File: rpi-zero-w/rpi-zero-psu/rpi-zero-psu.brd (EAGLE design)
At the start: 58 x 30 mm, 21 parts, among them J1 M20X2, J2 POWER_JACKPTH, Q1 DMG2305UX, Q2 DMG2302UK-7, U2 MP2307-MODULE, U4 DMMT5401

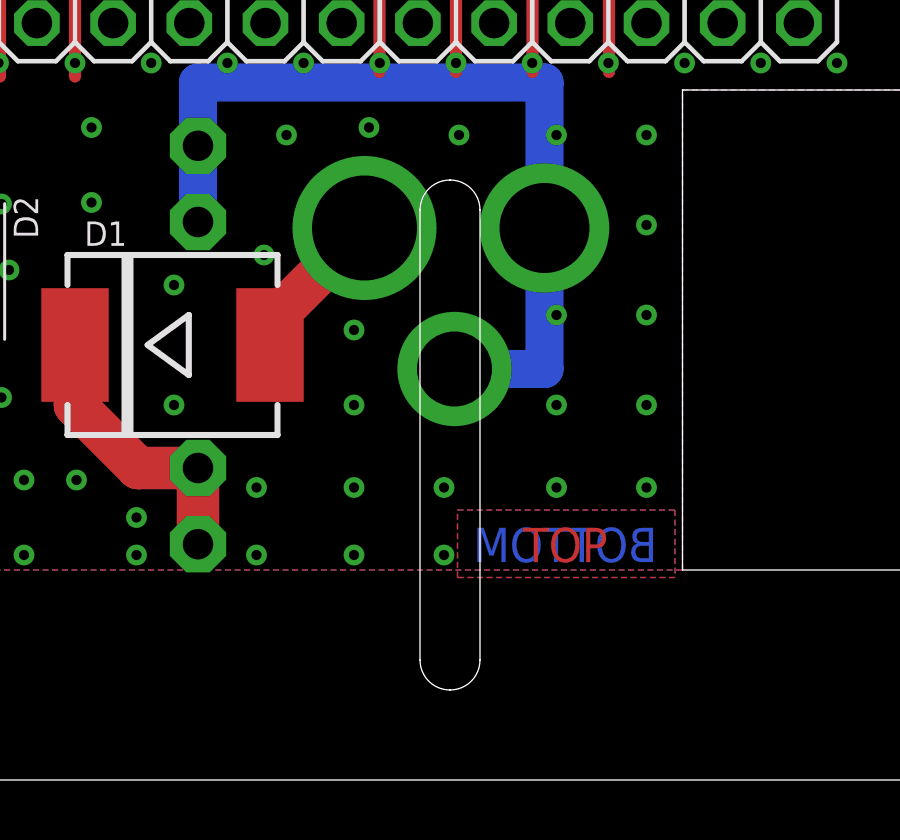
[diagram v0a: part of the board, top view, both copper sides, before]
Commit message: rpi-zero-psu: removed milling layer
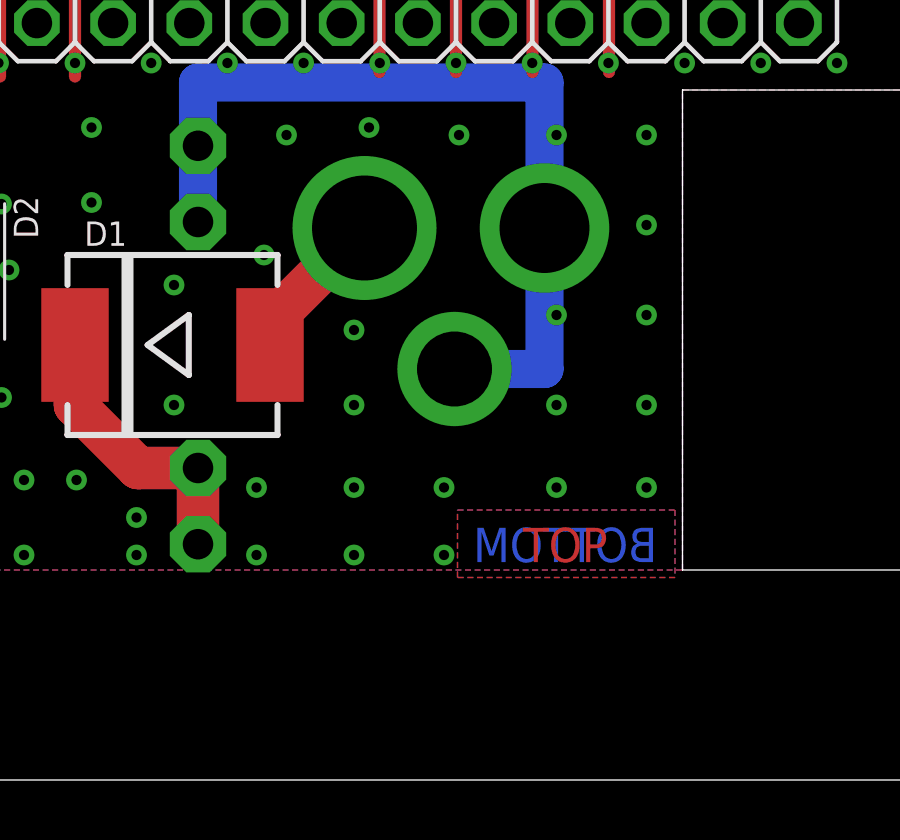
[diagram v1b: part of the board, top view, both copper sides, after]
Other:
- outline, holes or cut-outs redrawn
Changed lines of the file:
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@@
 <layer number="44" name="Drills" color="7" fill="1" visible="no" active="yes"/>
 <layer number="45" name="Holes" color="7" fill="1" visible="yes" active="yes"/>
-<layer number="46" name="Milling" color="3" fill="1" visible="no" active="yes"/>
+<layer number="46" name="Milling" color="3" fill="1" visible="yes" active="yes"/>
 <layer number="47" name="Measures" color="7" fill="1" visible="no" active="yes"/>
 <layer number="48" name="Document" color="7" fill="1" visible="no" active="yes"/>
@@
 <circle x="61.5" y="3.5" radius="1.55" width="3.1" layer="42"/>
 <circle x="61.5" y="26.5" radius="1.55" width="3.1" layer="42"/>
-<wire x1="44" y1="19" x2="44" y2="4" width="0" layer="46"/>
-<wire x1="46" y1="4" x2="45" y2="3" width="0" layer="46" curve="-90"/>
-<wire x1="44" y1="4" x2="45" y2="3" width="0" layer="46" curve="90"/>
-<wire x1="45" y1="20" x2="44" y2="19" width="0" layer="46" curve="90"/>
-<wire x1="45" y1="20" x2="46" y2="19" width="0" layer="46" curve="-90"/>
-<wire x1="46" y1="19" x2="46" y2="4" width="0" layer="46"/>
 <text x="57.25" y="0.75" size="1.016" layer="22" ratio="16" rot="MR0">Rev 1A</text>
 <text x="57.25" y="3.1" size="1.778" layer="22" ratio="16" rot="MR0">RPI Zero PSU HAT</text>
